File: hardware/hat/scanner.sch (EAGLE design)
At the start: 24 parts, among them U1 CAT24C32WI-GT3, U2 TPS61165DBV

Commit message: fixed issues with 1.0
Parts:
- added R8, R9: 3k9, resistor:R-EU_M0805
- C1: value 100nF -> 4.7μF
- C3: value 4.7μF -> 1μF
- C4: value 1μF -> 100nF
- POWER: value 2.1MMJACKTHM -> PJ-102AH; device adafruit:2.1MMJACKTHM -> PJ-102AH:PJ-102AH
- R1, R2: value 3k9 -> 330
- R3: value 3k9 -> 10k
- R5, R6: value 330 -> (none)
- R7: value 10k -> 3k9
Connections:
- net N$7 renamed LED_COMP
- removed net N$10: C4.1, D1.C, LED1.A
- new net N$2: C3.1, D1.C, LED1.A
- net +3V3: now also C4.1, R5.2, R7.2, R8.2, R9.1; no longer C1.1, R1.2, R2.2, R3.1
- net +5V: now also C1.1, POWER.1; no longer C3.1, POWER.TIP
- net EEPROM_SCL: now also GPIO.28, R8.1; no longer GPIO.27, R2.1
- net EEPROM_SDA: now also GPIO.27, R7.1; no longer GPIO.28, R1.1
- net EEPROM_WP: now also R9.2; no longer R3.2
- net GND: now also POWER.2, POWER.3, R6.1; no longer POWER.RING, POWER.RING_SW
- net LED3: now also R1.1; no longer R5.1
- net LED4: now also R2.1; no longer R6.1
- net LED5: now also R3.1; no longer R7.1
- net LED_CTRL: now also R5.1, R6.2
- net N$13: now also R1.2; no longer R5.2
- net N$17: now also R2.2; no longer R6.2
- net N$18: now also R3.2; no longer R7.2
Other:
- note added: "EEPROM"
- note added: "IO"
- note added: "LED Driver"
- note removed: "Checked by:"
- note removed: "Drawn by:"
- note removed: "Edwin Svensson"
- note removed: "shopper.ink"
- note removed: "v1.0"

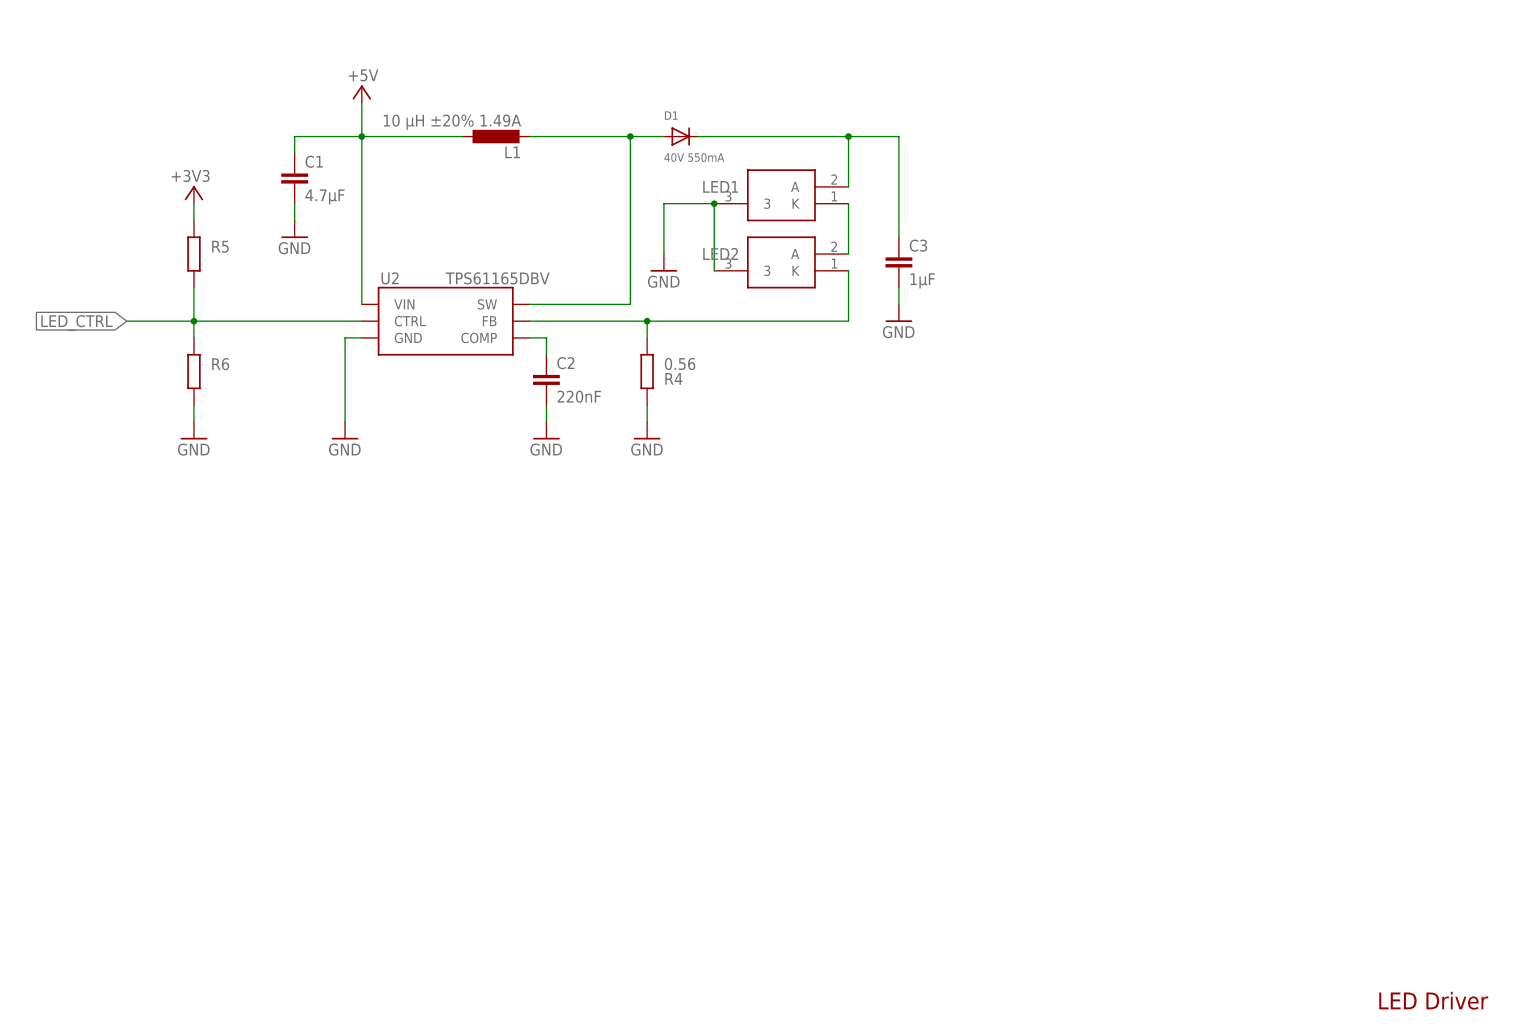
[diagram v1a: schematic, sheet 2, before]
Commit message: add 3V3 regulator
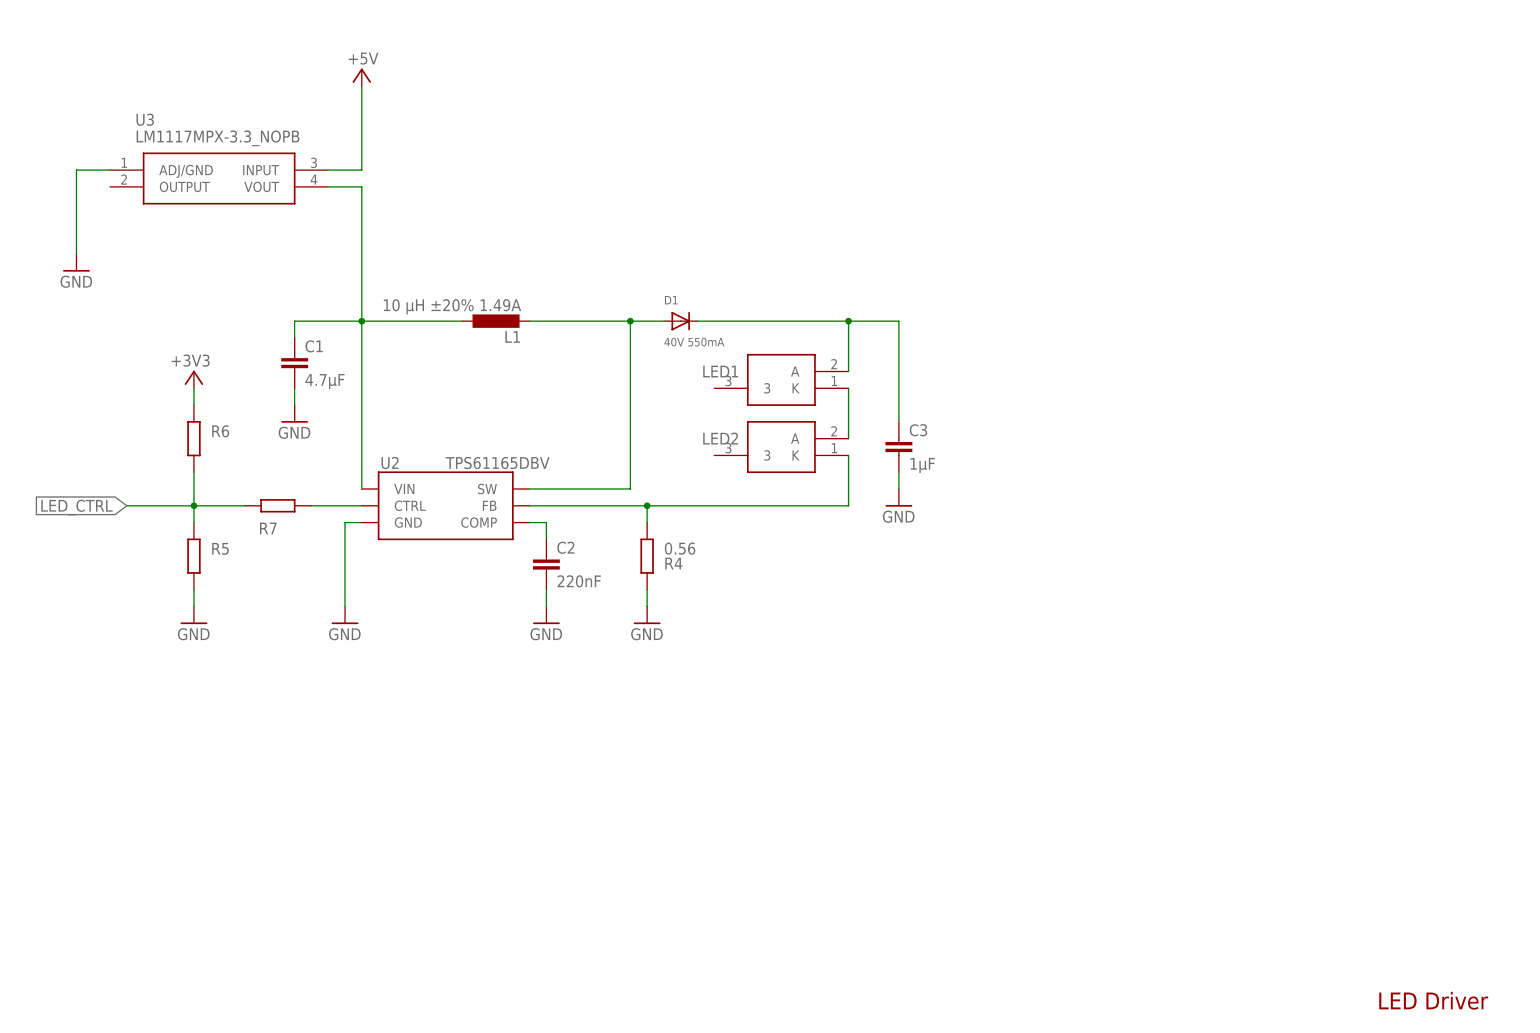
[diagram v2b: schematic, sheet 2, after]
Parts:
- added R10: 3k9, resistor:R-EU_M0805
- added U3: LM1117MPX-3.3_NOPB, LM1117MPX-3.3_NOPB:LM1117MPX-3.3_NOPB
- R7: value 3k9 -> (none)
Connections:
- new net LED_CTRL1: R7.1, U2.CTRL
- new net VCC: C1.1, L1.1, U2.VIN, U3.VOUT
- net +3V3: now also R10.1, R6.2, R9.2; no longer R5.2, R7.2, R9.1
- net +5V: now also U3.INPUT; no longer C1.1, L1.1, U2.VIN
- net EEPROM_SCL: now also R9.1; no longer R8.1
- net EEPROM_SDA: now also R8.1; no longer R7.1
- net EEPROM_WP: now also R10.2; no longer R9.2
- net GND: now also R5.1, U3.ADJ/GND; no longer LED1.3, LED2.3, R6.1
- net LED_CTRL: now also R5.2, R6.1, R7.2; no longer R5.1, R6.2, U2.CTRL
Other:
- moved on the sheet: C1, C2, C3, D1, L1, LED1, LED2, R4, R5, R6, R8, R9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

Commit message: v1.1-d1
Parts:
- removed POWER: PJ-102AH, PJ-102AH:PJ-102AH
- added C5, C6: (no value), rcl:CPOL-EUCT6032
- added J1: PJ-102AH, PJ-102AH:PJ-102AH
- R5, R6: value (none) -> Optional
- R7: value (none) -> 0
- U3: value LM1117MPX-3.3_NOPB -> (none); device LM1117MPX-3.3_NOPB:LM1117MPX-3.3_NOPB -> SparkFun-IC-Power:V_REG_LM1117SOT223
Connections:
- net +5V: now also C6.+, J1.1, U3.IN; no longer POWER.1, U3.INPUT
- net GND: now also C5.-, C6.-, J1.2, U3.ADJ; no longer POWER.2, POWER.3, U3.ADJ/GND
- net VCC: now also C5.+, U3.OUT, U3.OUT@1; no longer U3.VOUT
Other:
- moved on the sheet: TRIGGER-1, TRIGGER-2, TRIGGER-3
